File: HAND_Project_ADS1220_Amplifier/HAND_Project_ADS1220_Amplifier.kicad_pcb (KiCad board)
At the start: 2 copper layers, 14 parts, among them J1 Screw_Terminal_01x04, J2 Conn_01x03_Pin, J3 Conn_01x03_Pin, J4 Conn_01x01_Pin, J5 Conn_01x01_Pin, U1 ADS1220IPWR

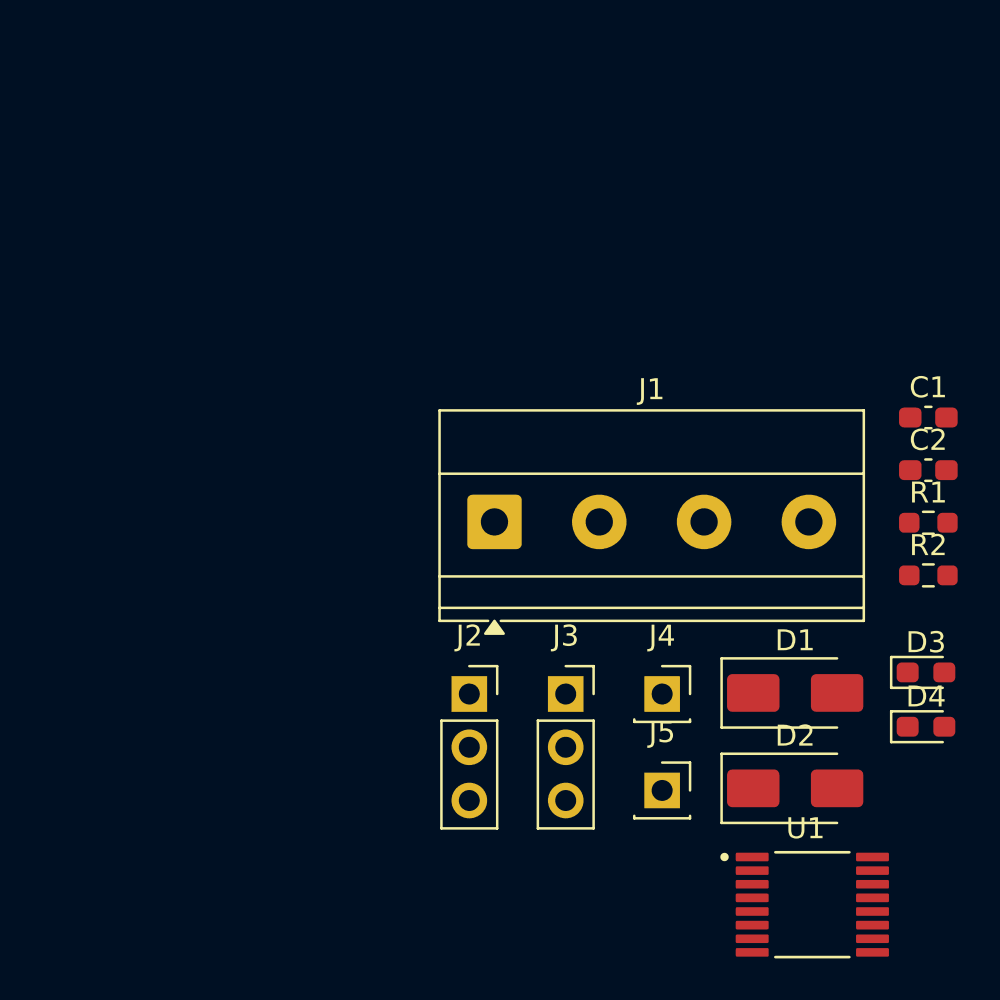
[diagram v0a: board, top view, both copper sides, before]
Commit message: Attempted to trace PCB... became very confused
Attempting to trace PCB was very difficult. I think I may need to use more vias and perhaps the underside of the board as well because my components are surface mounted.
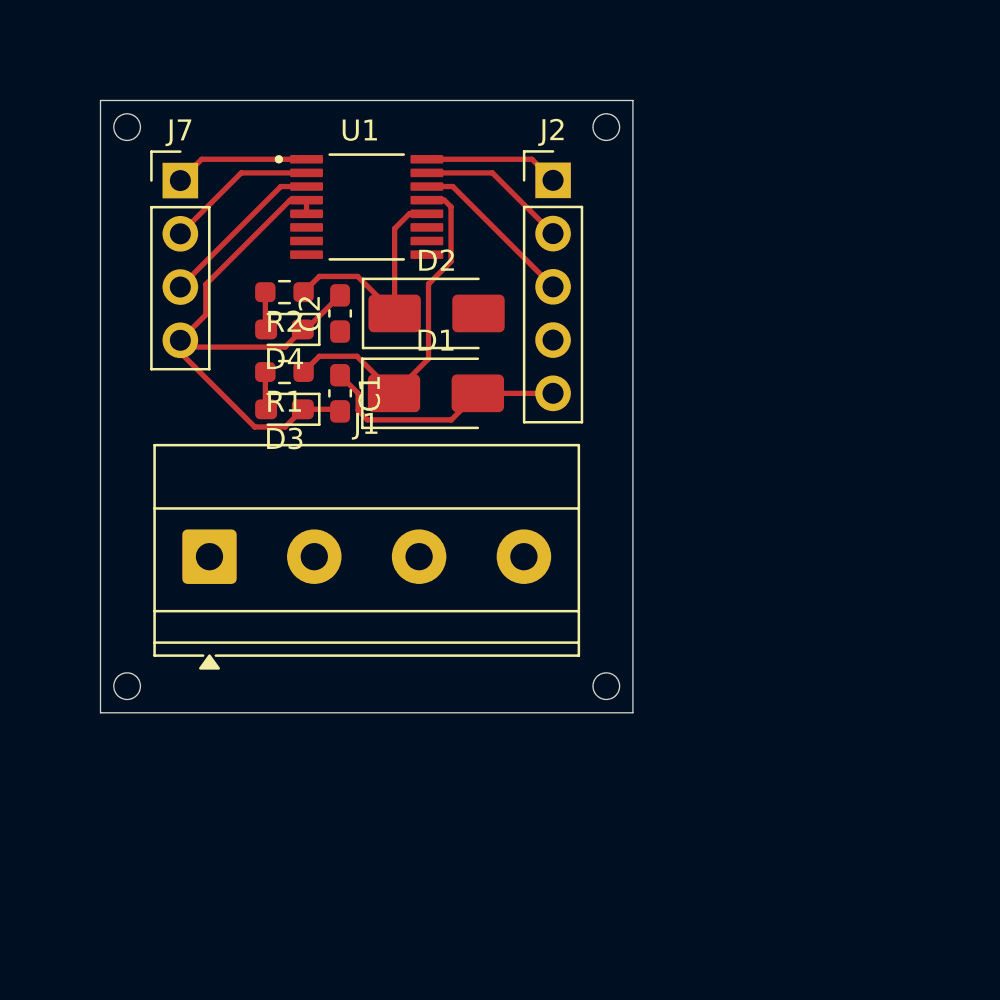
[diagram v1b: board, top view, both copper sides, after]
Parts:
- removed J3: Conn_01x03_Pin, Connector_PinSocket_2.54mm:PinSocket_1x03_P2.54mm_Vertical
- removed J4, J5: Conn_01x01_Pin, Connector_PinSocket_2.54mm:PinSocket_1x01_P2.54mm_Vertical
- added J7: Conn_01x04_Pin, Connector_PinHeader_2.54mm:PinHeader_1x04_P2.54mm_Vertical, F.Cu at (129.5, 71.1)
- J2: value Conn_01x03_Pin -> Conn_01x05_Pin; footprint Connector_PinSocket_2.54mm:PinSocket_1x03_P2.54mm_Vertical -> Connector_PinHeader_2.54mm:PinHeader_1x05_P2.54mm_Vertical
- moved U1 39.5 mm to (138.4, 72.4)
- moved D4 36.0 mm to (134.5, 78.2), turned to 180 degrees
- moved R2 33.6 mm to (134.5, 76.5), turned to 180 degrees
- moved D3 33.1 mm to (134.5, 82.0), turned to 180 degrees
- moved R1 31.5 mm to (134.5, 80.3), turned to 180 degrees
- moved C2 29.0 mm to (137.2, 77.5), turned to 90 degrees
- moved D2 28.4 mm to (141.8, 77.5)
- moved C1 28.1 mm to (137.2, 81.3), turned to -90 degrees
- moved J2 24.8 mm to (147.3, 71.1)
- moved D1 22.3 mm to (141.7, 81.3)
- moved J1 13.7 mm to (130.9, 89.1)
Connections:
- U1 pad 1: Net-(J2-Pin_1) -> Net-(J7-Pin_1)
- U1 pad 14: Net-(J3-Pin_1) -> Net-(J2-Pin_3)
- U1 pad 15: Net-(J3-Pin_2) -> Net-(J2-Pin_2)
- U1 pad 16: Net-(J3-Pin_3) -> Net-(J2-Pin_1)
- U1 pad 2: Net-(J2-Pin_2) -> Net-(J7-Pin_2)
- U1 pad 3: Net-(J2-Pin_3) -> Net-(J7-Pin_3)
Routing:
- net GND: track 0.00 -> 29.1 mm
- net Net-(D1-K): track 0.00 -> 16.7 mm
- net 3.3V: track 0.00 -> 12.0 mm
- net Net-(D2-K): track 0.00 -> 11.3 mm
- net Net-(J7-Pin_3): track 0.00 -> 8.01 mm
- net Net-(J2-Pin_3): track 0.00 -> 8.00 mm
- net Net-(J7-Pin_2): track 0.00 -> 7.22 mm
- net Net-(J2-Pin_2): track 0.00 -> 7.22 mm
- net Net-(J7-Pin_1): track 0.00 -> 6.44 mm
- net Net-(J2-Pin_1): track 0.00 -> 6.44 mm
- net Net-(D4-A): track 0.00 -> 1.79 mm
- net Net-(D3-A): track 0.00 -> 1.79 mm
- net 5V: track 0.00 -> 1.06 mm
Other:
- board outline added: 25.4 x 29.2 mm

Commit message: Components Update
Update 1: 2x LPF RC filters added for both Analog Signals from the J1 screw into the ADS

Update 2: 1x Power Connector pin for 5V and GND added as suggested by Luke
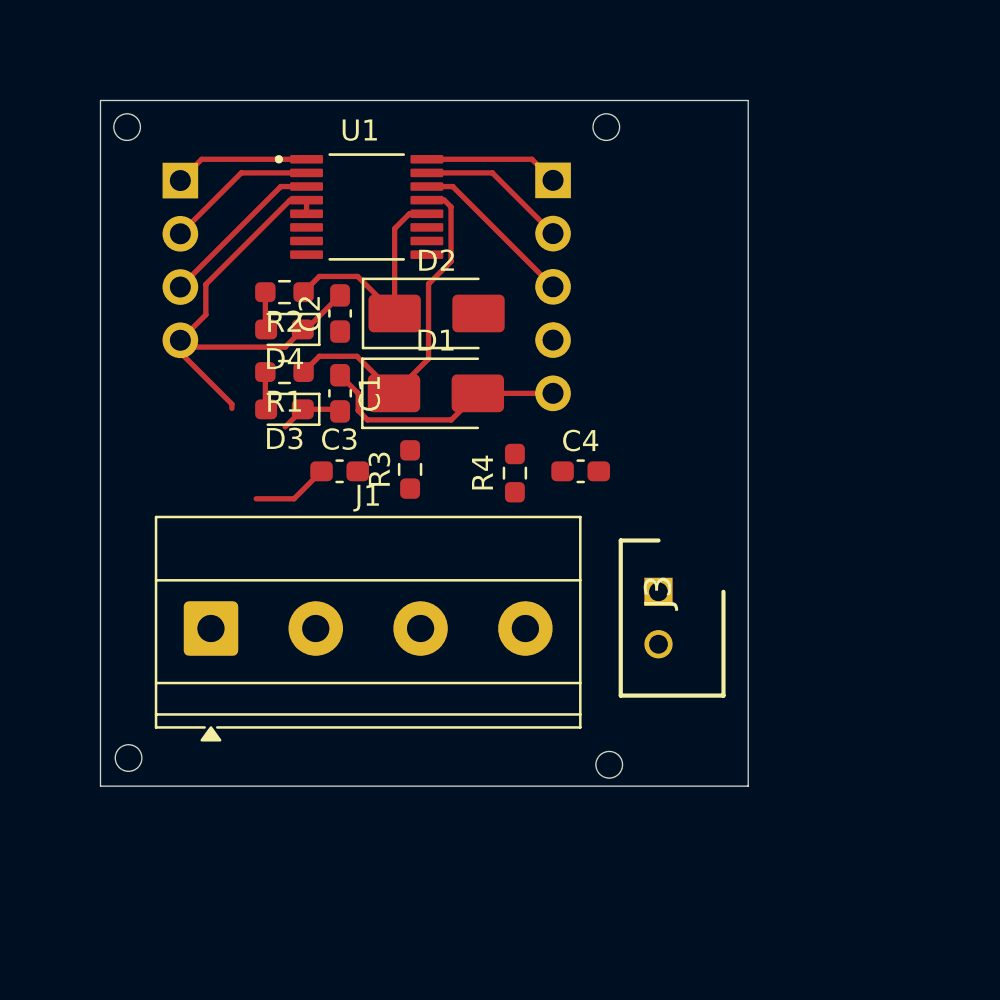
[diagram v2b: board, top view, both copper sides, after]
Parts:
- added C3: 15 nF, Capacitor_SMD:C_0603_1608Metric_Pad1.08x0.95mm_HandSolder, F.Cu at (137.1, 85.0)
- added C4: 15 nF, Capacitor_SMD:C_0603_1608Metric_Pad1.08x0.95mm_HandSolder, F.Cu at (148.6, 85.0)
- added J3: 22-03-5025, SamacSys_Parts:SHDR2W70P0X250_1X2_740X490X590P, F.Cu at (152.3, 90.8)
- added R3: 10k, Resistor_SMD:R_0603_1608Metric_Pad0.98x0.95mm_HandSolder, F.Cu at (140.5, 84.9)
- added R4: 10k, Resistor_SMD:R_0603_1608Metric_Pad0.98x0.95mm_HandSolder, F.Cu at (145.5, 85.1)
- J2, J7: moved to B.Cu
- moved J1 3.43 mm to (131.0, 92.5)
- turned J2 to 180 degrees
- turned J7 to 180 degrees
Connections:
- U1 pad 10: Net-(J1-Pin_3) -> unconnected-(U1-AIN1-Pad10)
- U1 pad 11: Net-(J1-Pin_4) -> Net-(U1-AIN0/REFP1)
- U1 pad 6: unconnected-(U1-AIN3/REFN1-Pad6) -> Net-(U1-AIN3/REFN1)
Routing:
- net GND: track 29.1 -> 30.0 mm
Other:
- board size 25.4 x 29.2 mm -> 30.9 x 32.7 mm

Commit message: Eric's PCB (without teensy integration)
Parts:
- removed J3: 22-03-5025, SamacSys_Parts:SHDR2W70P0X250_1X2_740X490X590P
- moved C4 4.37 mm to (144.3, 84.9), turned to -90 degrees
- moved C3 2.05 mm to (139.2, 85.0), turned to -90 degrees
- moved R4 0.57 mm to (146.1, 84.9)
- moved R3 0.48 mm to (141.0, 85.0)
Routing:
- net Net-(U1-AIN3/REFN1): track 0.00 -> 21.4 mm, vias 0 -> 2
- net Net-(U1-AIN0/REFP1): track 0.00 -> 14.1 mm, vias 0 -> 2
- net Net-(J1-Pin_4): track 0.00 -> 6.67 mm
- net Net-(J1-Pin_3): track 0.00 -> 6.61 mm
- net GND: track 30.0 -> 34.7 mm
- net 5V: track 1.06 -> 2.73 mm
- net Net-(D1-K): track 16.7 -> 17.2 mm, vias 0 -> 2
- added copper zone on F.Cu, net 5V
- added copper zone on B.Cu, net GND
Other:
- board size 30.9 x 32.7 mm -> 25.4 x 33 mm

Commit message: Finished Organizing and Sectioning schematic
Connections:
- net Net-(D1-K) renamed /DVDD
- net Net-(D2-K) renamed /AVDD
- net Net-(J2-Pin_1) renamed /DIN
- net Net-(J2-Pin_2) renamed /DOUT
- net Net-(J2-Pin_3) renamed /DRDY
- net Net-(J7-Pin_1) renamed /SCLK
- net Net-(J7-Pin_2) renamed /CS
- net Net-(J7-Pin_3) renamed /CLK
- net Net-(U1-AIN0/REFP1) renamed /AIN0
- net Net-(U1-AIN3/REFN1) renamed /AIN3
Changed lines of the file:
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@@
 	(net 2 "GND")
 	(net 3 "5V")
-	(net 4 "Net-(D1-K)")
-	(net 5 "Net-(D2-K)")
+	(net 4 "/DVDD")
+	(net 5 "/AVDD")
 	(net 6 "Net-(D3-A)")
 	(net 7 "Net-(D4-A)")
 	(net 8 "Net-(J1-Pin_3)")
 	(net 9 "Net-(J1-Pin_4)")
-	(net 10 "Net-(J2-Pin_1)")
-	(net 11 "Net-(J2-Pin_3)")
-	(net 12 "Net-(J2-Pin_2)")
-	(net 13 "Net-(U1-AIN0{slash}REFP1)")
+	(net 10 "/DOUT")
+	(net 11 "/DIN")
+	(net 12 "/DRDY")
+	(net 13 "/AIN0")
 	(net 14 "unconnected-(U1-REFN0-Pad8)")
 	(net 15 "unconnected-(U1-AIN2-Pad7)")
 	(net 16 "unconnected-(U1-REFP0-Pad9)")
-	(net 17 "Net-(J7-Pin_1)")
-	(net 18 "Net-(J7-Pin_3)")
-	(net 19 "Net-(J7-Pin_2)")
-	(net 20 "Net-(U1-AIN3{slash}REFN1)")
+	(net 17 "/SCLK")
+	(net 18 "/CLK")
+	(net 19 "/CS")
+	(net 20 "/AIN3")
 	(net 21 "unconnected-(U1-AIN1-Pad10)")
 	(footprint "Capacitor_SMD:C_0603_1608Metric_Pad1.08x0.95mm_HandSolder"
@@
 			(layers "F.Cu" "F.Mask" "F.Paste")
 			(roundrect_rratio 0.25)
-			(net 20 "Net-(U1-AIN3{slash}REFN1)")
+			(net 20 "/AIN3")
 			(pintype "passive")
 		)
@@
 			(layers "F.Cu" "F.Mask" "F.Paste")
 			(roundrect_rratio 0.25)
-			(net 20 "Net-(U1-AIN3{slash}REFN1)")
+			(net 20 "/AIN3")
 			(pintype "passive")
 		)
@@
 			(layers "F.Cu" "F.Mask" "F.Paste")
 			(roundrect_rratio 0.25)
-			(net 13 "Net-(U1-AIN0{slash}REFP1)")
+			(net 13 "/AIN0")
 			(pintype "passive")
 		)
@@
 			(layers "F.Cu" "F.Mask" "F.Paste")
 			(roundrect_rratio 0.25)
-			(net 13 "Net-(U1-AIN0{slash}REFP1)")
+			(net 13 "/AIN0")
 			(pintype "passive")
 		)
@@
 			(layers "F.Cu" "F.Mask" "F.Paste")
 			(roundrect_rratio 0.125)
-			(net 17 "Net-(J7-Pin_1)")
+			(net 17 "/SCLK")
 			(pinfunction "SCLK")
 			(pintype "input")
@@
 			(layers "F.Cu" "F.Mask" "F.Paste")
 			(roundrect_rratio 0.125)
-			(net 19 "Net-(J7-Pin_2)")
+			(net 19 "/CS")
 			(pinfunction "~{CS}")
 			(pintype "input")
@@
 			(layers "F.Cu" "F.Mask" "F.Paste")
 			(roundrect_rratio 0.125)
-			(net 18 "Net-(J7-Pin_3)")
+			(net 18 "/CLK")
 			(pinfunction "CLK")
 			(pintype "input")
@@
 			(layers "F.Cu" "F.Mask" "F.Paste")
 			(roundrect_rratio 0.125)
-			(net 20 "Net-(U1-AIN3{slash}REFN1)")
+			(net 20 "/AIN3")
 			(pinfunction "AIN3/REFN1")
 			(pintype "input")
@@
 			(layers "F.Cu" "F.Mask" "F.Paste")
 			(roundrect_rratio 0.125)
-			(net 13 "Net-(U1-AIN0{slash}REFP1)")
+			(net 13 "/AIN0")
 			(pinfunction "AIN0/REFP1")
 			(pintype "input")
@@
 			(layers "F.Cu" "F.Mask" "F.Paste")
 			(roundrect_rratio 0.125)
-			(net 5 "Net-(D2-K)")
+			(net 5 "/AVDD")
 			(pinfunction "AVDD")
 			(pintype "power_in")
@@
 			(layers "F.Cu" "F.Mask" "F.Paste")
 			(roundrect_rratio 0.125)
-			(net 4 "Net-(D1-K)")
+			(net 4 "/DVDD")
 			(pinfunction "DVDD")
 			(pintype "power_in")
@@
 			(layers "F.Cu" "F.Mask" "F.Paste")
 			(roundrect_rratio 0.125)
-			(net 11 "Net-(J2-Pin_3)")
+			(net 12 "/DRDY")
 			(pinfunction "~{DRDY}")
 			(pintype "output")
@@
 			(layers "F.Cu" "F.Mask" "F.Paste")
 			(roundrect_rratio 0.125)
-			(net 12 "Net-(J2-Pin_2)")
+			(net 10 "/DOUT")
 			(pinfunction "DOUT/~{DRDY}")
 			(pintype "output")
@@
 			(layers "F.Cu" "F.Mask" "F.Paste")
 			(roundrect_rratio 0.125)
-			(net 10 "Net-(J2-Pin_1)")
+			(net 11 "/DIN")
 			(pinfunction "DIN")
 			(pintype "input")
@@
 			(layers "F.Cu" "F.Mask" "F.Paste")
 			(roundrect_rratio 0.25)
-			(net 4 "Net-(D1-K)")
+			(net 4 "/DVDD")
 			(pintype "passive")
 		)
@@
 			(layers "F.Cu" "F.Mask" "F.Paste")
 			(roundrect_rratio 0.1388888889)
-			(net 4 "Net-(D1-K)")
+			(net 4 "/DVDD")
 			(pinfunction "K")
 			(pintype "passive")
@@
 			(layers "F.Cu" "F.Mask" "F.Paste")
 			(roundrect_rratio 0.1388888889)
-			(net 5 "Net-(D2-K)")
+			(net 5 "/AVDD")
 			(pinfunction "K")
 			(pintype "passive")
@@
 			(layers "F.Cu" "F.Mask" "F.Paste")
 			(roundrect_rratio 0.25)
-			(net 5 "Net-(D2-K)")
+			(net 5 "/AVDD")
 			(pintype "passive")
 		)
@@
 			(layers "*.Cu" "*.Mask")
 			(remove_unused_layers no)
-			(net 17 "Net-(J7-Pin_1)")
+			(net 17 "/SCLK")
 			(pinfunction "Pin_1")
 			(pintype "passive")
@@
 			(layers "*.Cu" "*.Mask")
 			(remove_unused_layers no)
-			(net 19 "Net-(J7-Pin_2)")
+			(net 19 "/CS")
 			(pinfunction "Pin_2")
 			(pintype "passive")
@@
 			(layers "*.Cu" "*.Mask")
 			(remove_unused_layers no)
-			(net 18 "Net-(J7-Pin_3)")
+			(net 18 "/CLK")
 			(pinfunction "Pin_3")
 			(pintype "passive")
@@
 			(layers "*.Cu" "*.Mask")
 			(remove_unused_layers no)
-			(net 10 "Net-(J2-Pin_1)")
+			(net 11 "/DIN")
 			(pinfunction "Pin_1")
 			(pintype "passive")
@@
 			(layers "*.Cu" "*.Mask")
 			(remove_unused_layers no)
-			(net 12 "Net-(J2-Pin_2)")
+			(net 10 "/DOUT")
 			(pinfunction "Pin_2")
 			(pintype "passive")
@@
 			(layers "*.Cu" "*.Mask")
 			(remove_unused_layers no)
-			(net 11 "Net-(J2-Pin_3)")
+			(net 12 "/DRDY")
 			(pinfunction "Pin_3")
 			(pintype "passive")
@@
 	)
 	(segment
-		(start 141.3 70.115)
-		(end 146.315 70.115)
+		(start 141.3 70.765)
+		(end 144.425 70.765)
 		(width 0.254)
 		(layer "F.Cu")
@@
 	)
 	(segment
-		(start 146.315 70.115)
-		(end 147.32 71.12)
+		(start 144.425 70.765)
+		(end 147.32 73.66)
 		(width 0.254)
 		(layer "F.Cu")
@@
 	)
 	(segment
-		(start 142.535 71.415)
-		(end 147.32 76.2)
+		(start 141.3 70.115)
+		(end 146.315 70.115)
 		(width 0.254)
 		(layer "F.Cu")
@@
 	)
 	(segment
-		(start 141.3 71.415)
-		(end 142.535 71.415)
+		(start 146.315 70.115)
+		(end 147.32 71.12)
 		(width 0.254)
 		(layer "F.Cu")
@@
 	)
 	(segment
-		(start 141.3 70.765)
-		(end 144.425 70.765)
+		(start 142.535 71.415)
+		(end 147.32 76.2)
 		(width 0.254)
 		(layer "F.Cu")
@@
 	)
 	(segment
-		(start 144.425 70.765)
-		(end 147.32 73.66)
+		(start 141.3 71.415)
+		(end 142.535 71.415)
 		(width 0.254)
 		(layer "F.Cu")

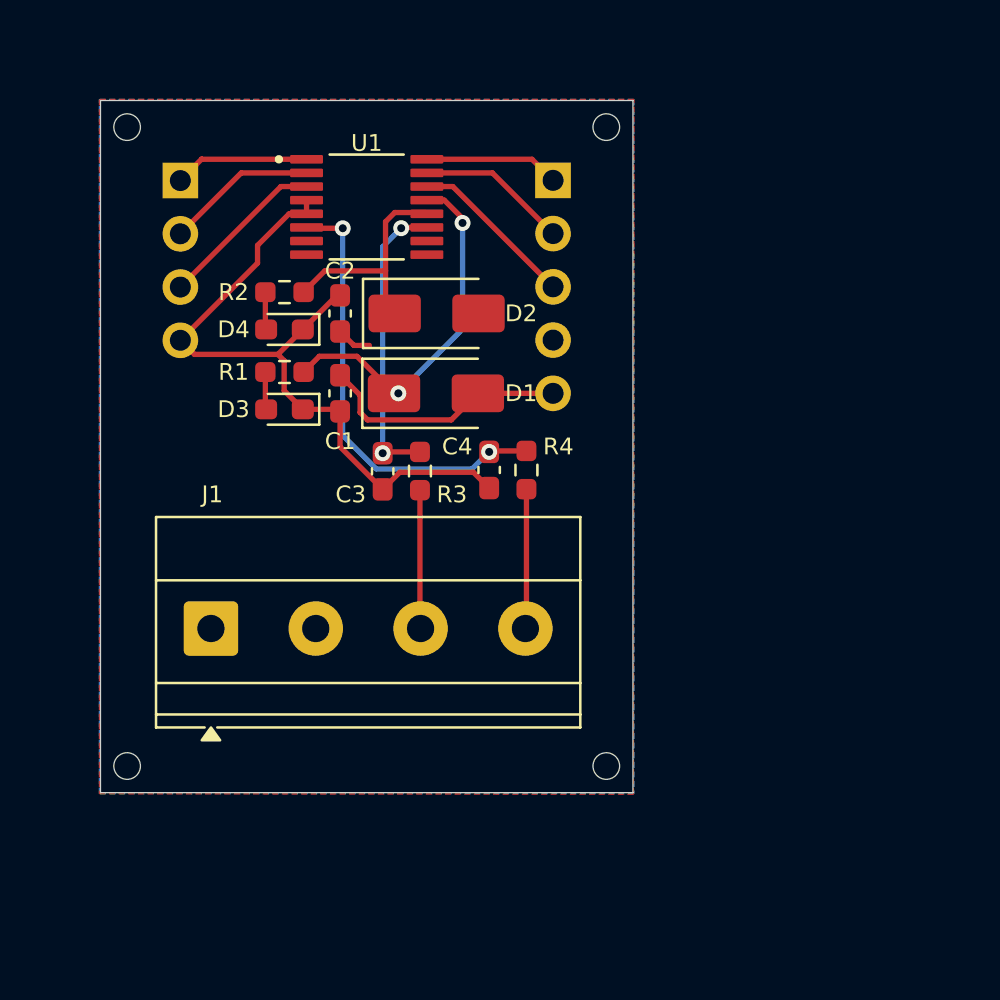
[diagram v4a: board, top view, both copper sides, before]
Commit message: Finished Design of PCB without teensy integration
Added external power supply, changed mounting holes to M3, generated gerber files, and the cost to manufacture 3 PCBs is $8.95
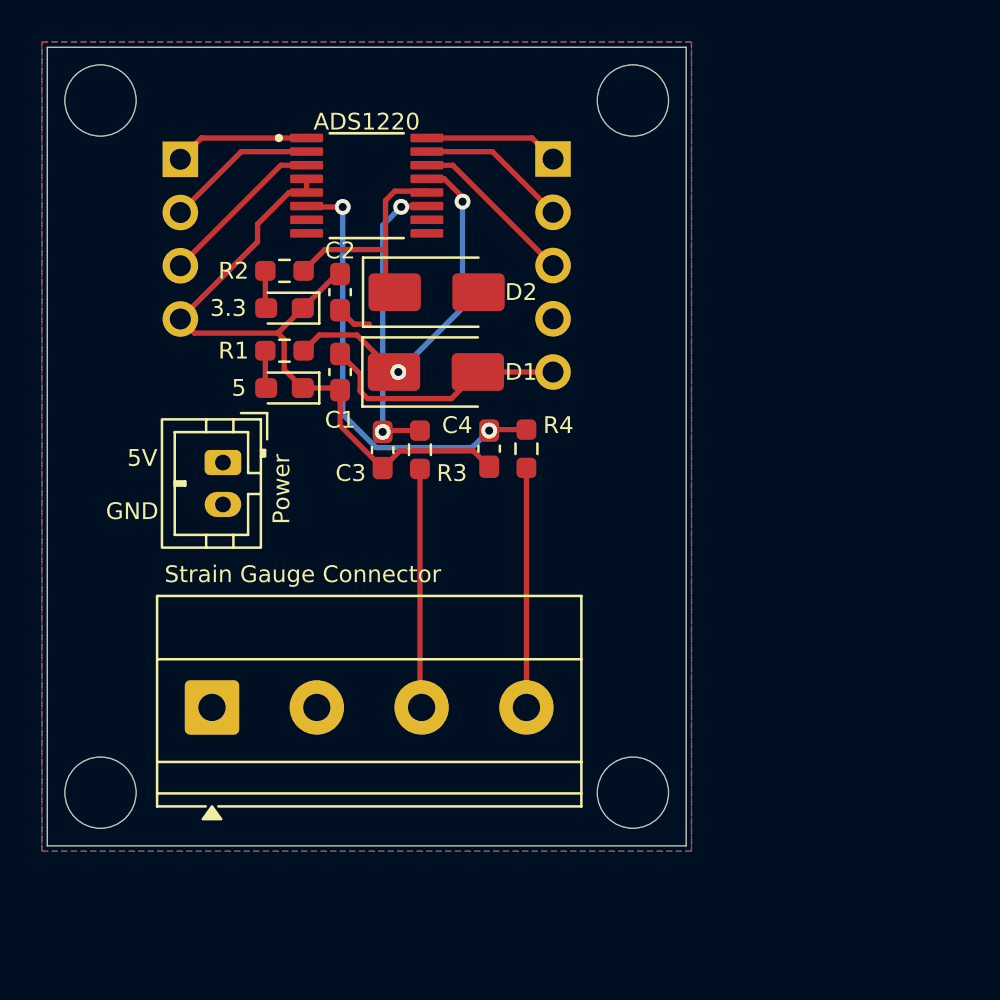
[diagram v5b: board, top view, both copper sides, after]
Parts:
- added Power: Conn_01x02_Pin, Connector_JST:JST_PH_B2B-PH-K_1x02_P2.00mm_Vertical, F.Cu at (131.6, 84.6)
- Strain Gauge Connector: renamed from J1
- moved Strain Gauge Connector 3.77 mm to (131.1, 96.3)
- moved 3.3 1.02 mm to (134.5, 77.2)
- moved 5 1.02 mm to (134.5, 81.0)
- moved ADS1220 1.02 mm to (138.4, 71.4)
- moved C1 1.02 mm to (137.2, 80.3)
- moved C2 1.02 mm to (137.2, 76.5)
- moved C3 1.02 mm to (139.2, 84.0)
- moved D1 1.02 mm to (141.7, 80.3)
- moved D2 1.02 mm to (141.8, 76.5)
- moved J2 1.02 mm to (147.3, 70.1)
- moved R3 1.02 mm to (141.0, 84.0)
- moved C4 1.02 mm to (144.3, 83.9)
- moved J7 1.02 mm to (129.5, 70.1)
- moved R1 1.02 mm to (134.5, 79.2)
- moved R2 1.02 mm to (134.5, 75.4)
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- renumbered D4 to 3.3, D3 to 5, U1 to ADS1220
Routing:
- net Net-(J1-Pin_3): track 6.61 -> 11.4 mm
- net Net-(J1-Pin_4): track 6.67 -> 11.4 mm
- net 5V: track 2.73 -> 1.67 mm
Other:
- board size 25.4 x 33 mm -> 30.5 x 38.1 mm
- board text added: "5V"
- board text added: "GND"
